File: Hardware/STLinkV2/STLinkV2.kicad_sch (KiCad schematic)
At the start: 66 parts, among them J1 USB_B_Micro, J2 SWD, J3 RS232, J4 ISP, J5 JTAG, U1 ME6211A33M3, U2 STM32F103CBT6, U3 AD8531ARTZ, U4 TXB0304RUT, U5 TXB0304RUT, Y1 8MHz

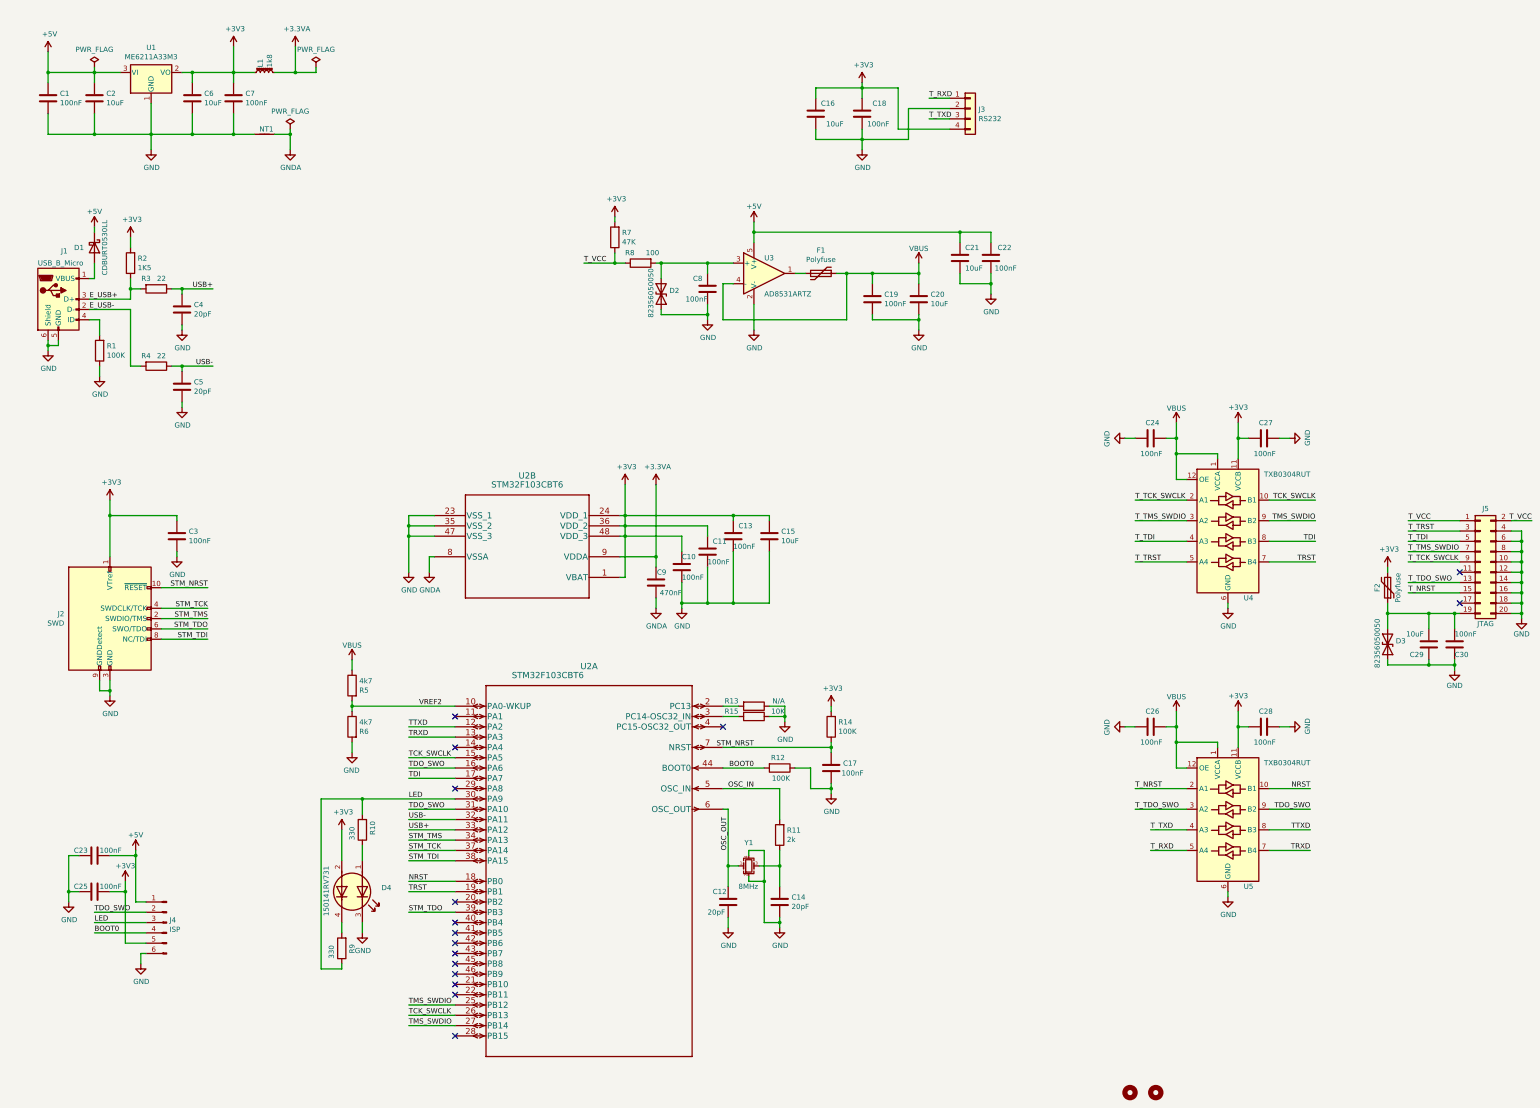
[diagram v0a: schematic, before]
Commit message: STLink/V2 ready for production
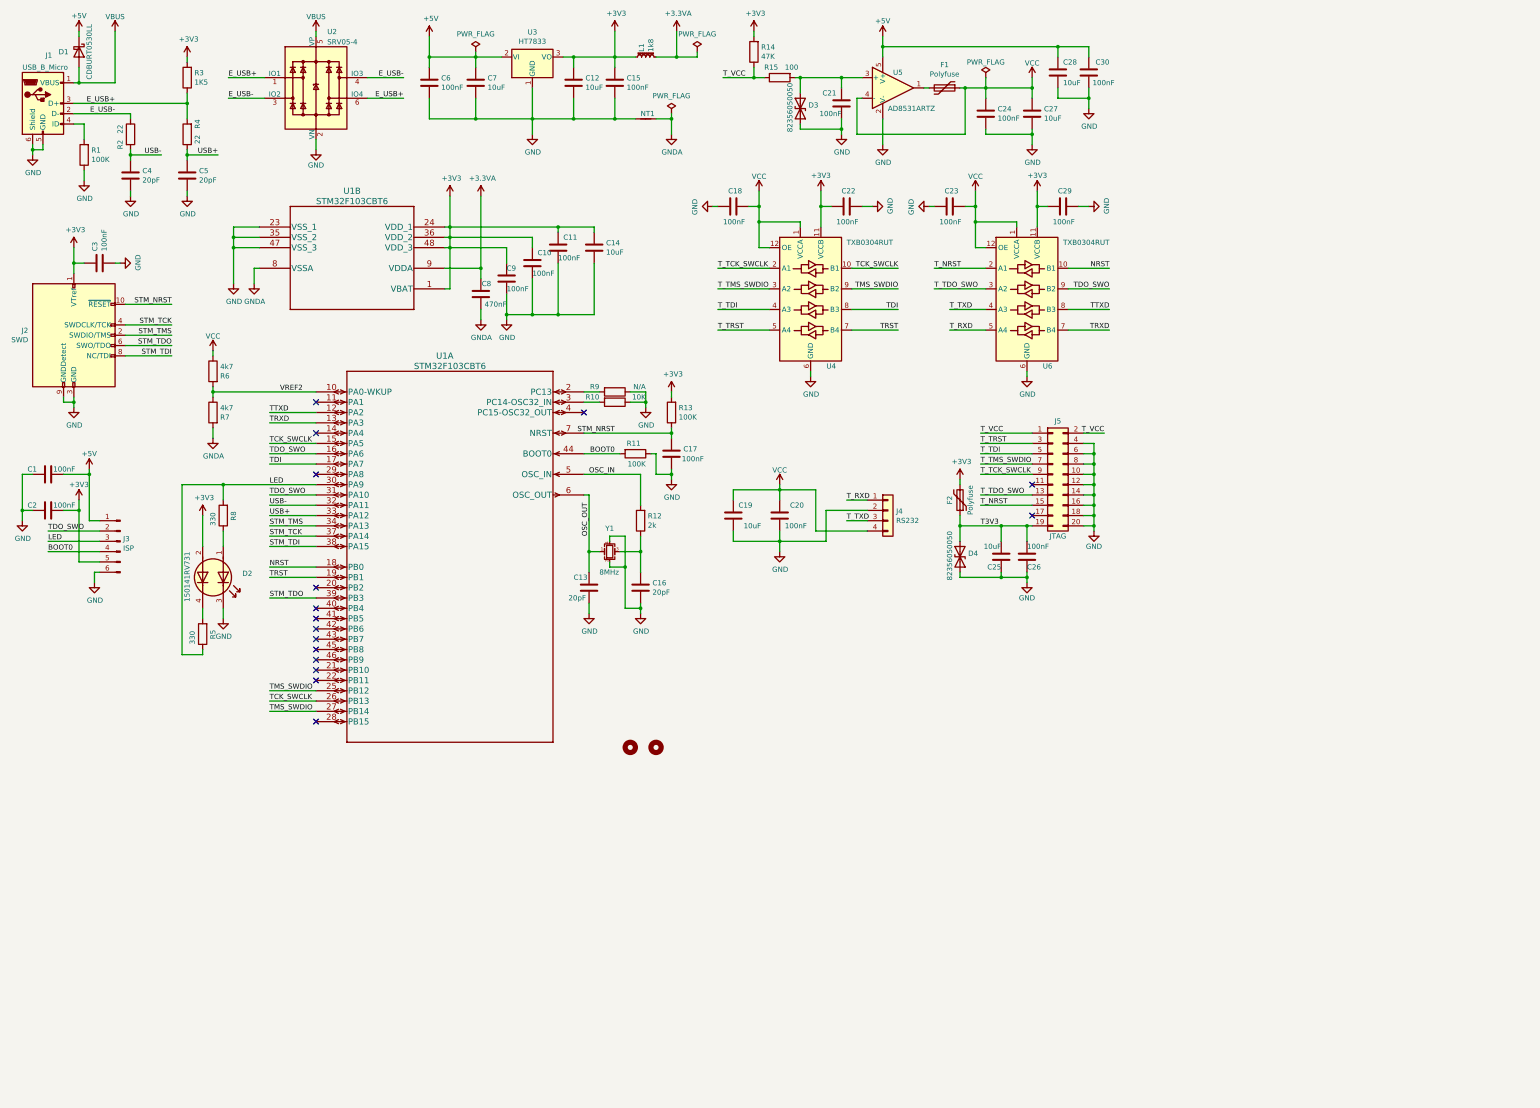
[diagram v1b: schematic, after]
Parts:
- added U2: SRV05-4, Package_TO_SOT_SMD:SOT-23-6, symbol Power_Protection:SRV05-4
- U3: renamed from U1; value ME6211A33M3 -> HT7833; footprint Package_TO_SOT_SMD:SOT-23 -> Package_TO_SOT_SMD:SOT-89-3; symbol Regulator_Linear:AMS1117-3.3 -> Regulator_Linear:AP2127R-3.3
- renumbered C23 to C1, C11 to C10, C13 to C11, C6 to C12, C12 to C13, C15 to C14, C7 to C15, C14 to C16, C24 to C18, C16 to C19, C25 to C2, C18 to C20, C8 to C21, C27 to C22, C26 to C23, C19 to C24, C29 to C25, C30 to C26, C20 to C27, C21 to C28, C28 to C29, C22 to C30, C5 to C4, C4 to C5, C1 to C6, C2 to C7, C9 to C8, C10 to C9, D4 to D2, D2 to D3, D3 to D4, J4 to J3, J3 to J4, R15 to R10, R12 to R11, R11 to R12, R14 to R13, R7 to R14, R8 to R15, R4 to R2, R2 to R3, R3 to R4, R9 to R5, R5 to R6, R6 to R7, R10 to R8, R13 to R9, U2 to U1, U3 to U5, U5 to U6
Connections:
- net +3V3: now also U3.3 (VO); no longer C19.1, C20.1, J4.4 (Pin_4), U3.2 (VO)
- net +5V: now also U3.2 (VI); no longer U3.3 (VI)
- net E_USB+: now also U2.1 (IO1), U2.6 (IO4)
- net E_USB-: now also R2.1, U2.3 (IO2), U2.4 (IO3); no longer R2.2
- net GND: now also U2.2 (VN); no longer R7.2
- net GNDA: now also R7.2
- net USB-: now also R2.2; no longer R2.1
- net VBUS: now also D1.2 (A), J1.1 (VBUS), U2.5 (VP); no longer C18.1, C23.1, C24.1, C27.1, F1.1, R6.1, U4.1 (VCCA), U4.12 (OE), U5.4 (-), U6.1 (VCCA), U6.12 (OE)
- net T3V3: now reaches C25.2, C26.1, D4.2 (A2), F2.1, J5.19 (Pin_19)
- new net VCC: C18.1, C19.1, C20.1, C23.1, C24.1, C27.1, F1.1, J4.4 (Pin_4), R6.1, U4.1 (VCCA), U4.12 (OE), U5.4 (-), U6.1 (VCCA), U6.12 (OE)
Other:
- moved on the sheet: C1, C10, C11, C12, C13, C14, C15, C16, C17, C18, C19, C2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

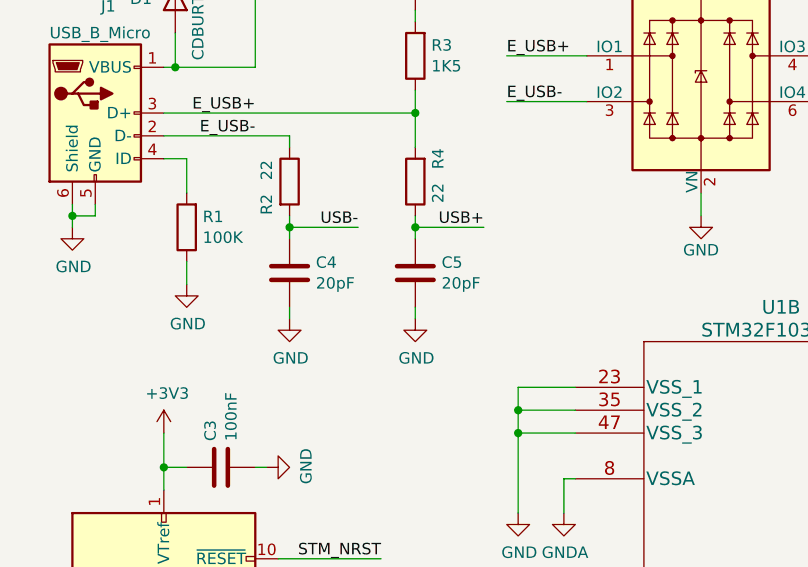
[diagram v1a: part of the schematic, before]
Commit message: Fine tune of USB EMI filter
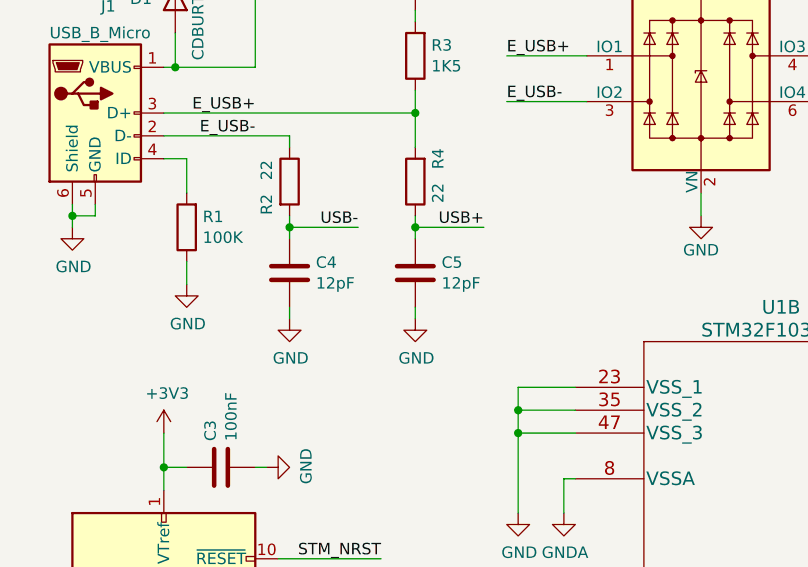
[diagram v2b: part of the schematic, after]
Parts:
- C4, C5: value 20pF -> 12pF
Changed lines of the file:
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@@
   (title_block
     (title "STLink-V2")
-    (date "2022-10-29")
+    (date "2022-11-09")
     (rev "1")
     (company "Mathias Gruber")
@@
       (effects (font (size 1.27 1.27)) (justify left))
     )
-    (property "Value" "20pF" (id 1) (at 58.801 55.753 0)
+    (property "Value" "12pF" (id 1) (at 58.801 55.753 0)
       (effects (font (size 1.27 1.27)) (justify left))
     )
@@
       (effects (font (size 1.27 1.27)) (justify left))
     )
-    (property "Value" "20pF" (id 1) (at 44.831 55.753 0)
+    (property "Value" "12pF" (id 1) (at 44.831 55.753 0)
       (effects (font (size 1.27 1.27)) (justify left))
     )
@@
     )
     (path "/00000000-0000-0000-0000-000061321b50"
-      (reference "C4") (unit 1) (value "20pF") (footprint "Capacitor_SMD:C_0603_1608Metric")
+      (reference "C4") (unit 1) (value "12pF") (footprint "Capacitor_SMD:C_0603_1608Metric")
     )
     (path "/00000000-0000-0000-0000-0000611a1c8a"
-      (reference "C5") (unit 1) (value "20pF") (footprint "Capacitor_SMD:C_0603_1608Metric")
+      (reference "C5") (unit 1) (value "12pF") (footprint "Capacitor_SMD:C_0603_1608Metric")
     )
     (path "/00000000-0000-0000-0000-000060d63f23"

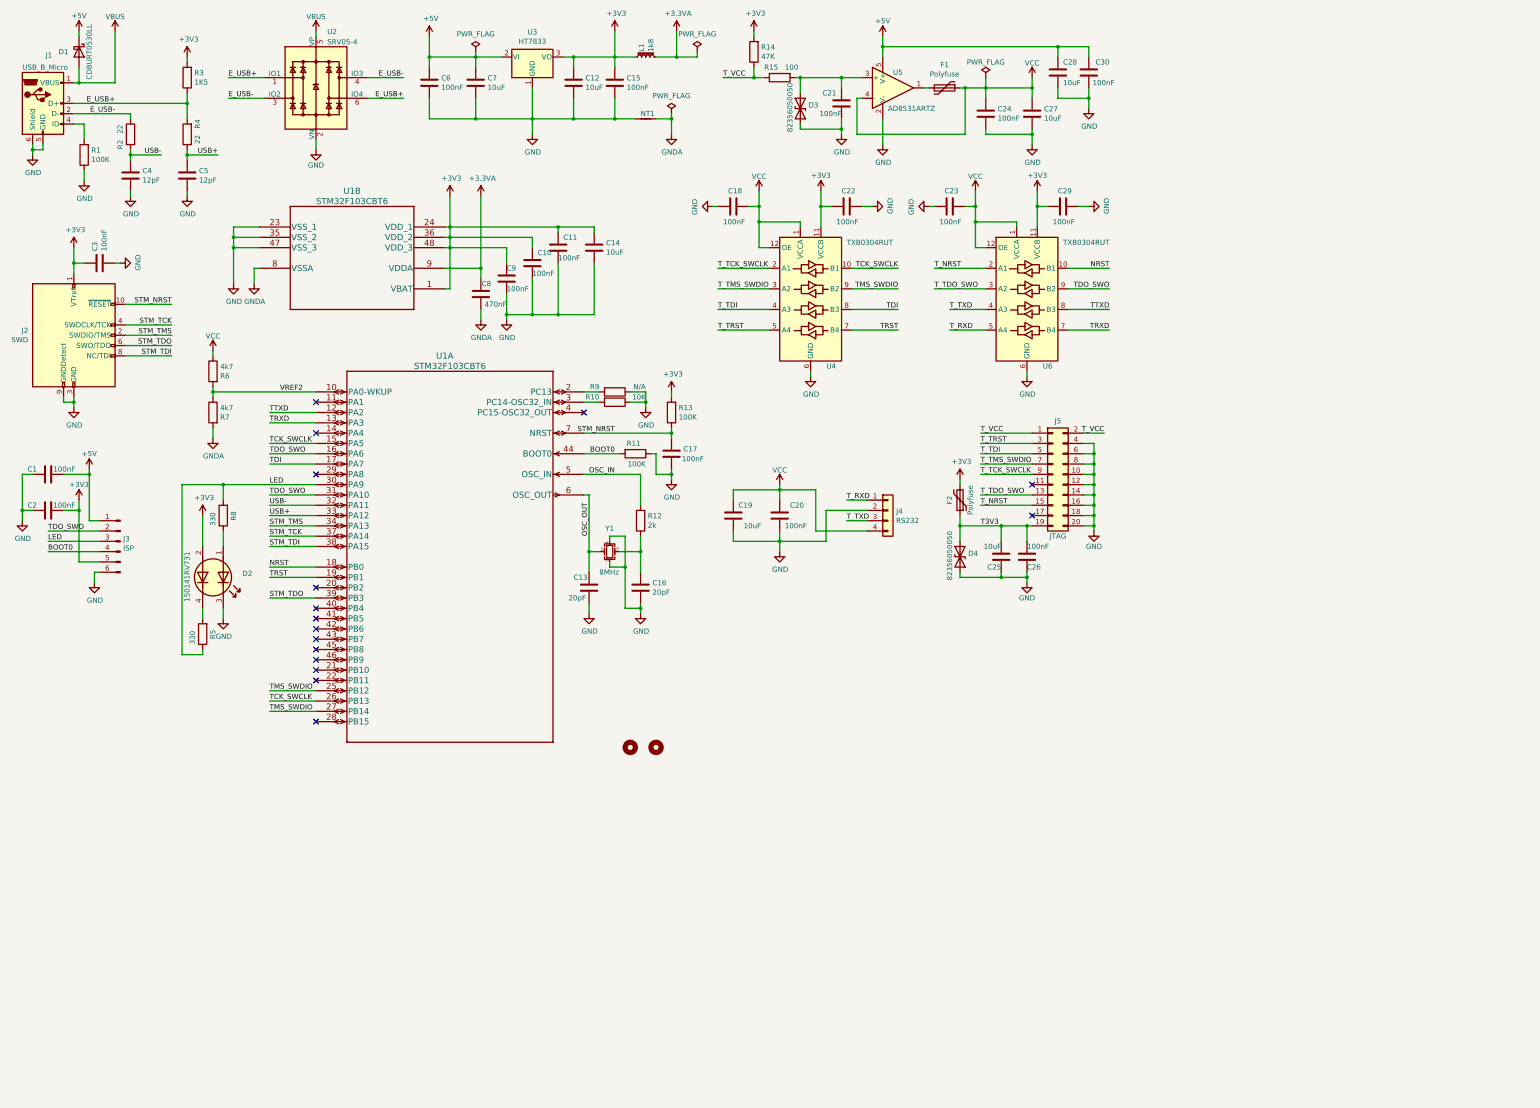
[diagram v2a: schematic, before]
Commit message: STLink V2 hardware review
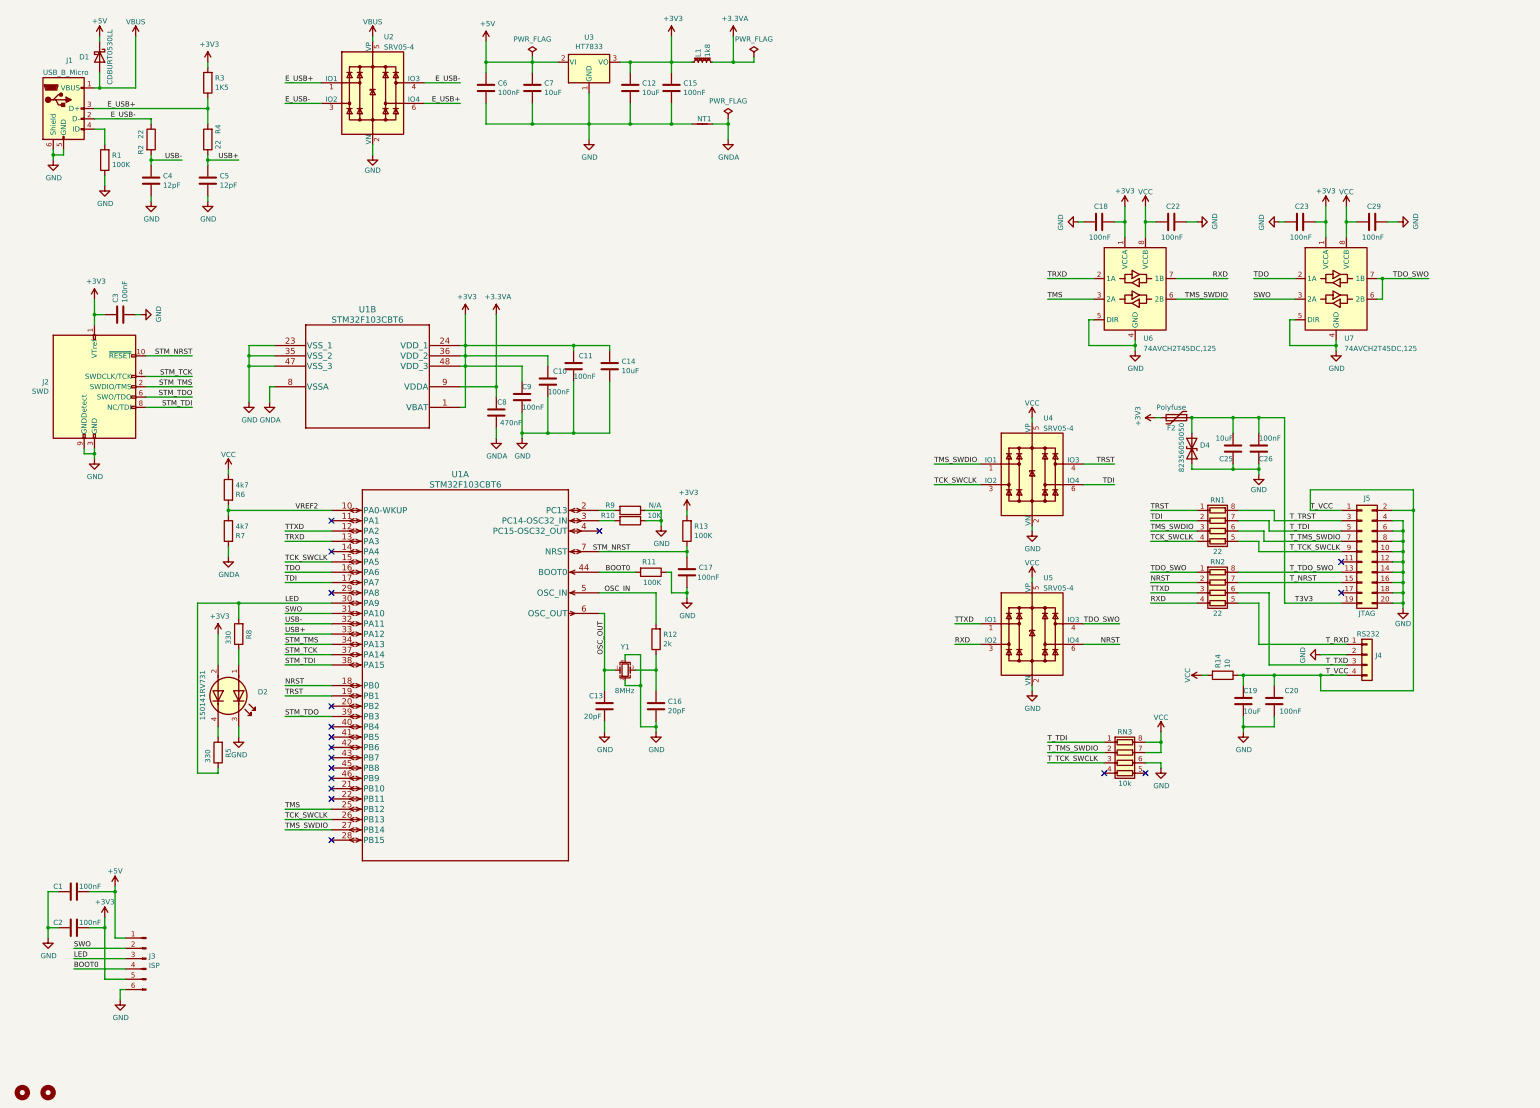
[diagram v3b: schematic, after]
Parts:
- removed C21, C24, C30: 100nF, Capacitor_SMD:C_0603_1608Metric, symbol Device:C
- removed C27, C28: 10uF, Capacitor_SMD:C_0603_1608Metric, symbol Device:C
- removed D3: 82356050050, Diode_SMD:D_0603_1608Metric, symbol Diode:ESD9B5.0ST5G
- removed F1: Polyfuse, Fuse:Fuse_0603_1608Metric, symbol Device:Polyfuse
- removed R15: 100, Resistor_SMD:R_0603_1608Metric, symbol Device:R
- removed U4, U6: TXB0304RUT, Package_DFN_QFN:Texas_R_PUQFN-N12, symbol Logic_LevelTranslator:TXB0304RUT
- removed U5: AD8531ARTZ, Package_TO_SOT_SMD:SOT-23-5, symbol AD8531ARTZ-REEL7:AD8531ARTZ
- added RN1, RN2: 22, Resistor_SMD:R_Array_Convex_4x0402, symbol Device:R_Pack04
- added RN3: 10k, Resistor_SMD:R_Array_Convex_4x0402, symbol Device:R_Pack04
- added U4, U5: SRV05-4, Package_TO_SOT_SMD:SOT-23-6, symbol Power_Protection:SRV05-4
- added U6, U7: 74AVCH2T45DC,125, Package_SO:VSSOP-8_2.3x2mm_P0.5mm, symbol Logic_LevelTranslator:74LVC2T45DC
- R14: value 47K -> 10; Descr 47kΩ ±1% 1/16W ±100ppm/℃ 0402 Chip Resistor - Surface Mount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 -> 100kΩ ±1% 1/16W ±100ppm/℃ 0402 Chip Resistor - Surface Moun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; LCSC C25792 -> C25741
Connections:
- net +3V3: now also C18.1, C23.1, U6.1 (VCCA), U7.1 (VCCA); no longer C22.2, C29.2, R14.2
- net GND: now also RN3.6 (R3.2), U4.2 (VN), U5.2 (VN), U6.4 (GND), U6.5 (DIR), U7.4 (GND), U7.5 (DIR)
- net NRST: now also RN2.2 (R2.1), U5.6 (IO4)
- net TCK_SWCLK: now also RN1.4 (R4.1), U4.3 (IO2)
- net TDI: now also RN1.2 (R2.1), U4.6 (IO4)
- net TDO_SWO: now also RN2.1 (R1.1), U5.4 (IO3), U7.6 (2B), U7.7 (1B); no longer J3.2 (Pin_2), U1.16 (PA6), U1.31 (PA10)
- net TMS_SWDIO: now also RN1.3 (R3.1), U4.1 (IO1), U6.6 (2B); no longer U1.25 (PB12)
- net TRST: now also RN1.1 (R1.1), U4.4 (IO3)
- net TRXD: now also U6.2 (1A)
- net TTXD: now also RN2.3 (R3.1), U5.1 (IO1)
- net T_NRST: now also RN2.7 (R2.2)
- net T_RXD: now also RN2.5 (R4.2)
- net T_TCK_SWCLK: now also RN1.5 (R4.2), RN3.3 (R3.1)
- net T_TDI: now also RN1.7 (R2.2), RN3.1 (R1.1)
- net T_TDO_SWO: now also RN2.8 (R1.2)
- net T_TMS_SWDIO: now also RN1.6 (R3.2), RN3.2 (R2.1)
- net T_TRST: now also RN1.8 (R1.2)
- net T_TXD: now also RN2.6 (R3.2)
- net T_VCC: now also C19.1, C20.1, J4.4 (Pin_4)
- net VCC: now also C22.2, C29.2, R14.2, RN3.7 (R2.2), RN3.8 (R1.2), U4.5 (VP), U5.5 (VP), U6.8 (VCCB), U7.8 (VCCB); no longer C18.1, C19.1, C20.1, C23.1, J4.4 (Pin_4)
- new net RXD: RN2.4 (R4.1), U5.3 (IO2), U6.7 (1B)
- new net SWO: J3.2 (Pin_2), U1.31 (PA10), U7.3 (2A)
- new net TDO: U1.16 (PA6), U7.2 (1A)
- new net TMS: U1.25 (PB12), U6.3 (2A)
- no-connect marks 16 -> 18
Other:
- moved on the sheet: C1, C10, C11, C12, C13, C14, C15, C16, C17, C18, C19, C2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
